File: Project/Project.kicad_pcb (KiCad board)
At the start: 2 copper layers, 15 parts, among them J4 Screw_Terminal_01x02, J5 Screw_Terminal_01x03, K1 JQC-3FF-005-1Z, Q2 MPSA42, U2 NE555D

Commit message: completed finishing
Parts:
- C3: footprint Capacitor_THT:CP_Radial_D10.0mm_P2.50mm -> Capacitor_THT:CP_Radial_D5.0mm_P2.00mm
- D3: footprint Diode_SMD:D_MELF -> Diode_SMD:D_MicroMELF
- D5, D6: footprint LED_SMD:LED_0201_0603Metric -> LED_SMD:LED_0805_2012Metric
- D7: footprint Diode_SMD:D_MiniMELF -> Diode_SMD:D_MicroMELF
- J4: footprint TerminalBlock_Phoenix:TerminalBlock_Phoenix_MKDS-1-2-3.81_1x02_P3.81mm_Horizontal -> TerminalBlock_Phoenix:TerminalBlock_Phoenix_MPT-0,5-2-2.54_1x02_P2.54mm_Horizontal
- K1: value JQC-3FF-005-1Z -> Relay_SPDT
- U2: footprint Package_DIP:DIP-8_W7.62mm -> Package_SO:SO-8_3.9x4.9mm_P1.27mm
- moved D5 75.5 mm to (99.0, 60.9), turned to 90 degrees
- moved J4 74.3 mm to (94.0, 56.5), turned to -90 degrees
- moved D3 69.2 mm to (99.0, 53.2), turned to 90 degrees
- moved C2 69.2 mm to (99.0, 57.0), turned to 90 degrees
- moved C4 65.8 mm to (102.5, 53.0)
- moved D6 59.6 mm to (113.9, 53.0)
- moved U2 59.5 mm to (108.9, 55.6), turned to 90 degrees
- moved R4 58.7 mm to (113.9, 55.5)
- moved R5 58.6 mm to (113.9, 58.0)
- moved RV2 55.7 mm to (107.6, 62.5)
- moved C3 45.8 mm to (102.0, 57.0)
- moved Q2 38.5 mm to (113.8, 61.0)
- moved D7 34.1 mm to (112.2, 64.0)
- moved K1 30.9 mm to (117.8, 59.0)
- moved J5 17.4 mm to (140.0, 61.6), turned to 90 degrees
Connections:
- K1 pad 1: (no net) -> Net-(J5-Pin_2)
- K1 pad 2: (no net) -> Net-(J5-Pin_3)
- K1 pad 3: (no net) -> VCC
- K1 pad 4: (no net) -> Net-(D7-A)
- K1 pad 5: (no net) -> Net-(J5-Pin_1)
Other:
- board outline added: 57.5 x 17 mm
- copper layers 2 -> 4
- board text added: "CB"
- board text added: "CK"
- board text added: "COM"
- board text added: "GND"
- board text added: "Time controlled relay"
- board text added: "VCC"

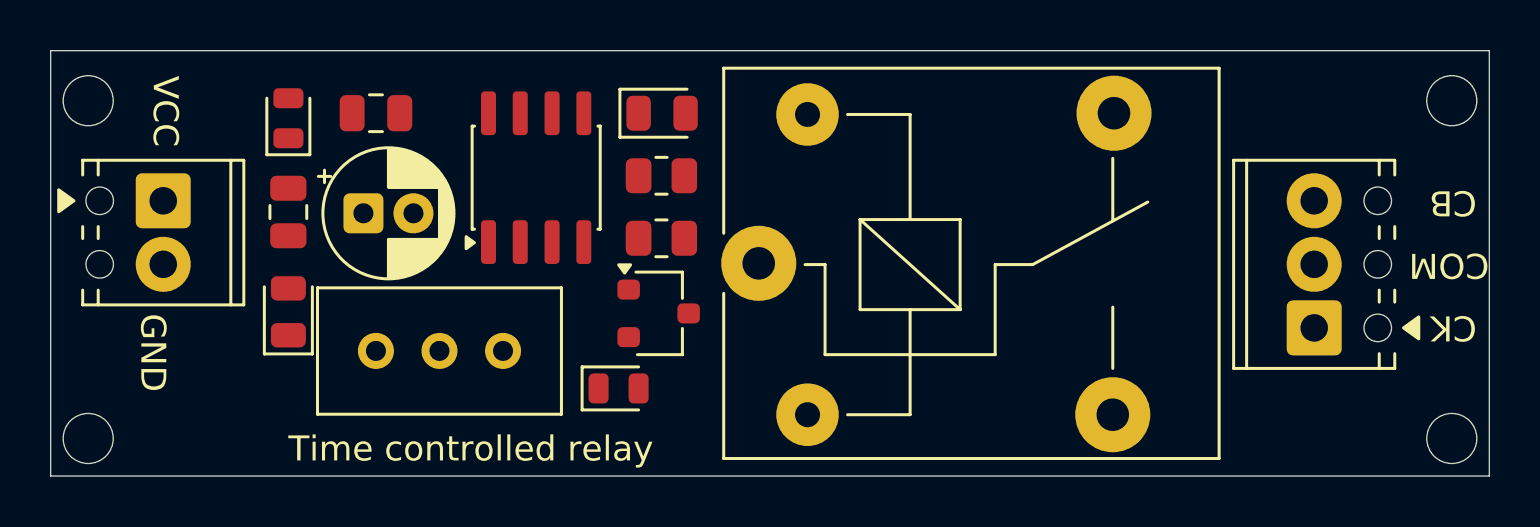
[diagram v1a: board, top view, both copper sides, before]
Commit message: Groundplane added
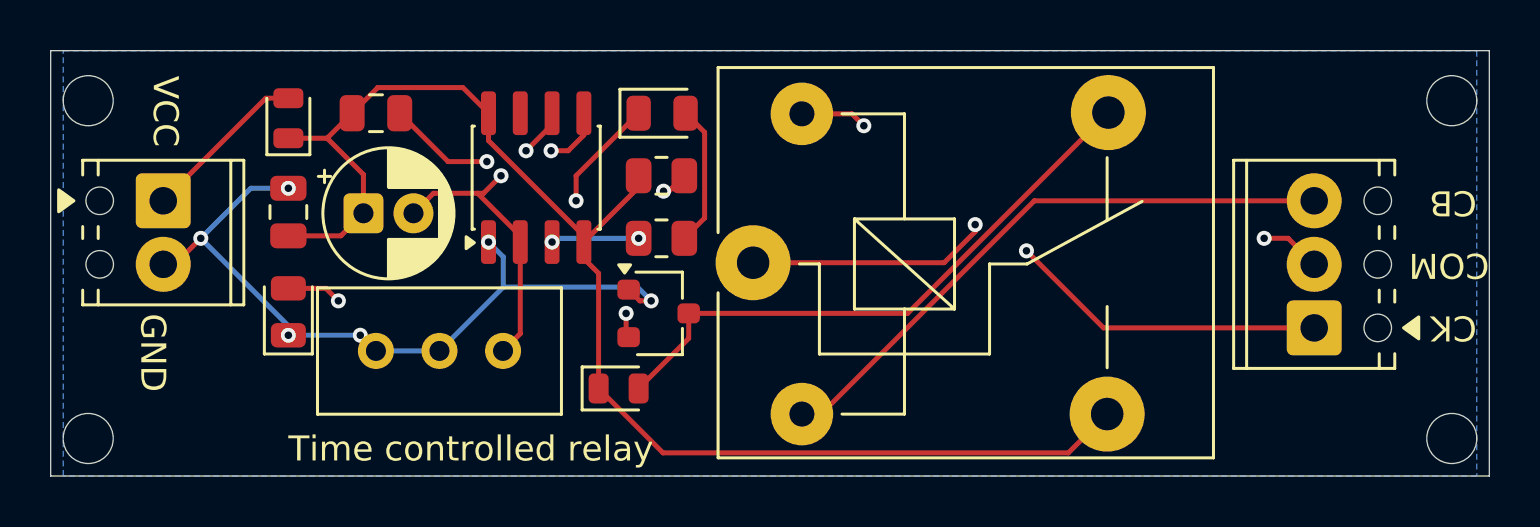
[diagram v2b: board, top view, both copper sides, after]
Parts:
- moved K1 0.23 mm to (117.6, 59.0)
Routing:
- net VCC: track 0.00 -> 54.7 mm
- net GNDD: track 0.00 -> 31.3 mm, vias 0 -> 6
- net Net-(J5-Pin_1): track 0.00 -> 24.0 mm, vias 0 -> 2
- net Net-(J5-Pin_3): track 0.00 -> 24.0 mm
- net Net-(D7-A): track 0.00 -> 23.9 mm
- net Net-(J5-Pin_2): track 0.00 -> 23.9 mm, vias 0 -> 2
- net Net-(D5-A): track 0.00 -> 18.1 mm, vias 0 -> 2
- net Net-(U2-THRES): track 0.00 -> 14.8 mm, vias 0 -> 2
- net Net-(D6-K): track 0.00 -> 10.9 mm, vias 0 -> 2
- net Net-(U2-CONT): track 0.00 -> 9.97 mm, vias 0 -> 2
- net Net-(D3-A): track 0.00 -> 6.70 mm
- net Net-(D6-A): track 0.00 -> 5.65 mm
- net Net-(U2-OUT): track 0.00 -> 3.52 mm, vias 0 -> 2
- added copper zone on B.Cu, net GNDD

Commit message: Complete end project
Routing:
- added copper zone on In2.Cu, net GNDD
- removed copper zone on B.Cu, net GNDD
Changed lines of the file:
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@@
 		(capping no)
 		(filling no)
+		(zone_defaults)
 		(pcbplotparams
-			(layerselection 0x00000000_00000000_55555555_5755f5ff)
+			(layerselection 0x00000000_00000000_55557fdf_57ffffff)
 			(plot_on_all_layers_selection 0x00000000_00000000_00000000_00000000)
 			(disableapertmacros no)
@@
 			(outputformat 1)
 			(mirror no)
-			(drillshape 1)
+			(drillshape 0)
 			(scaleselection 1)
 			(outputdirectory "")
@@
 	(zone
 		(net "GNDD")
-		(layer "B.Cu")
-		(name "GND")
+		(layer "In2.Cu")
 		(hatch edge 0.5)
 		(connect_pads
@@
 		)
 		(min_thickness 0.25)
-		(fill
+		(fill yes
 			(thermal_gap 0.5)
 			(thermal_bridge_width 0.5)
@@
 		(polygon
 			(pts
-				(xy 90 50.5) (xy 146.5 50.5) (xy 146.5 67.5) (xy 90 67.5)
+				(xy 89.5 50.5) (xy 147 50.5) (xy 147 67.5) (xy 89.5 67.5)
 			)
 		)
